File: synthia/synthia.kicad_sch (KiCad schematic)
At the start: 87 parts, among them J1 MJ-63022B, J2 SJ3-35083C-TR, J3 PJ-007, J4 SDS-50J, Q1 IRF9540N, U1 TLV272IP, U2 STM32H750ZBT6, U3 LD1117V33

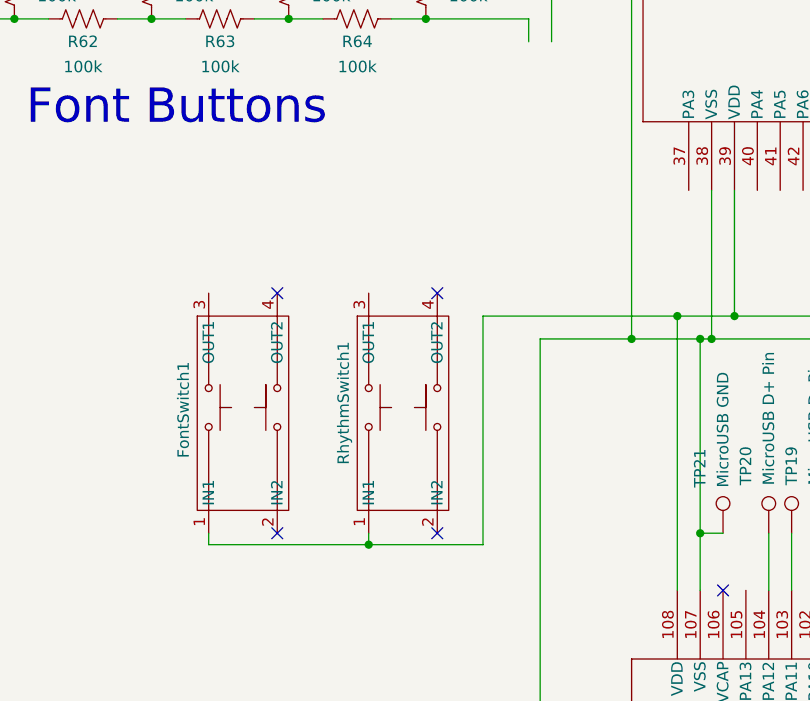
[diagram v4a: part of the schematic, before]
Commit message: added all 3D models for the footprints into the pcb design, fixed some DRC errors
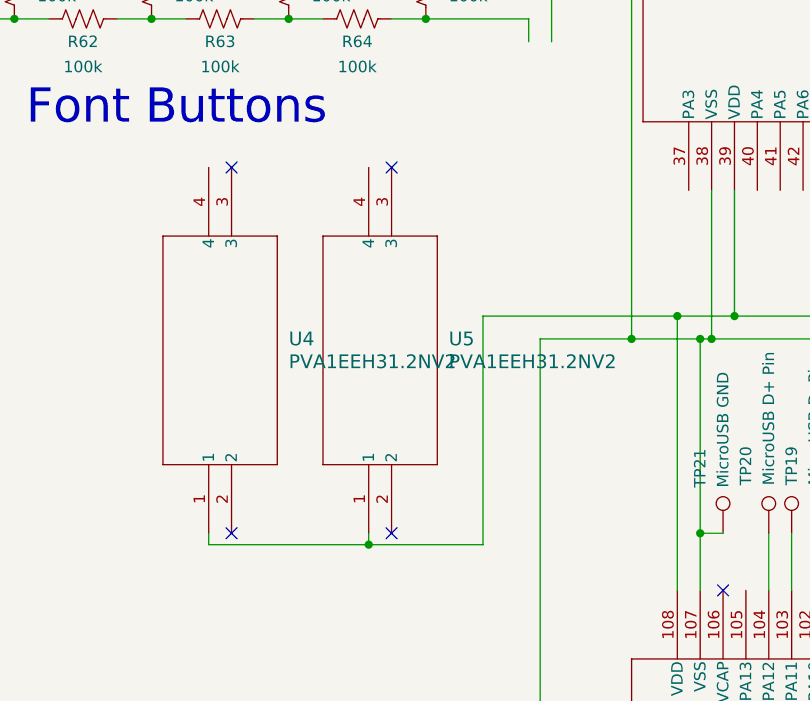
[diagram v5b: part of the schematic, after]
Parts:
- removed FontSwitch1, RhythmSwitch1: (no value), Synthia_footprint_library:Latching Switch, symbol Synthia_Symbol_Library:Latching_switch
- added U4, U5: PVA1EEH31.2NV2, SWITCH_H31.2NV2, symbol Synthia_Symbol_Library:PVA1EEH31.2NV2
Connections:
- net +3.3V: now also U4.1, U5.1
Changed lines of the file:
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@@
 	)
 	(no_connect
-		(at 60.96 199.39)
+		(at 55.88 199.39)
 	)
 	(no_connect
@@
 	)
 	(no_connect
-		(at 78.74 172.72)
+		(at 73.66 158.75)
 	)
 	(no_connect
@@
 	)
 	(no_connect
-		(at 60.96 172.72)
+		(at 55.88 158.75)
 	)
 	(no_connect
@@
 	)
 	(no_connect
-		(at 78.74 199.39)
+		(at 73.66 199.39)
 	)
 	(no_connect
@@
 	)
 	(symbol
-		(lib_id "Synthia_Symbol_Library:Latching_switch")
-		(at 62.23 181.61 0)
+		(lib_id "Synthia_Symbol_Library:PVA1EEH31.2NV2")
+		(at 53.34 199.39 90)
 		(unit 1)
 		(body_style 1)
@@
 		(in_pos_files yes)
 		(dnp no)
-		(property "Reference" "FontSwitch1"
-			(at 50.546 185.674 90)
+		(fields_autoplaced yes)
+		(property "Reference" "U4"
+			(at 62.23 177.7999 90)
 			(show_name no)
 			(do_not_autoplace no)
 			(effects
 				(font
-					(size 1.27 1.27)
+					(size 1.524 1.524)
 				)
+				(justify right)
 			)
 		)
-		(property "Value" ""
-			(at 62.23 181.61 0)
+		(property "Value" "PVA1EEH31.2NV2"
+			(at 62.23 180.3399 90)
 			(show_name no)
 			(do_not_autoplace no)
 			(effects
 				(font
-					(size 1.27 1.27)
+					(size 1.524 1.524)
 				)
+				(justify right)
 			)
 		)
-		(property "Footprint" "Synthia_footprint_library:Latching Switch"
-			(at 62.23 181.61 0)
+		(property "Footprint" "SWITCH_H31.2NV2"
+			(at 53.34 199.39 0)
 			(hide yes)
 			(show_name no)
@@
 				(font
 					(size 1.27 1.27)
+					(italic yes)
 				)
 			)
 		)
-		(property "Datasheet" ""
-			(at 62.23 181.61 0)
+		(property "Datasheet" "PVA1EEH31.2NV2"
+			(at 53.34 199.39 0)
 			(hide yes)
 			(show_name no)
@@
 				(font
 					(size 1.27 1.27)
+					(italic yes)
 				)
 			)
 		)
 		(property "Description" ""
-			(at 62.23 181.61 0)
+			(at 53.34 199.39 0)
 			(hide yes)
 			(show_name no)
@@
 			)
 		)
-		(pin "2"
-		)
 		(pin "3"
 		)
-		(pin "4"
-		)
 		(pin "1"
 		)
+		(pin "2"
+		)
+		(pin "4"
+		)
 		(instances
 			(project "synthia"
 				(path "/b7ca07b0-c23c-4333-a610-582d2798793b"
-					(reference "FontSwitch1")
+					(reference "U4")
 					(unit 1)
 				)
@@
 	)
 	(symbol
-		(lib_id "Synthia_Symbol_Library:Latching_switch")
-		(at 80.01 181.61 0)
-		(unit 1)
-		(body_style 1)
-		(exclude_from_sim no)
-		(in_bom yes)
-		(on_board yes)
-		(in_pos_files yes)
-		(dnp no)
-		(property "Reference" "RhythmSwitch1"
-			(at 68.326 191.77 90)
-			(show_name no)
-			(do_not_autoplace no)
-			(effects
-				(font
-					(size 1.27 1.27)
-				)
-				(justify left)
-			)
-		)
-		(property "Value" ""
-			(at 80.01 181.61 0)
-			(show_name no)
-			(do_not_autoplace no)
-			(effects
-				(font
-					(size 1.27 1.27)
-				)
-			)
-		)
-		(property "Footprint" "Synthia_footprint_library:Latching Switch"
-			(at 80.01 181.61 0)
-			(hide yes)
-			(show_name no)
-			(do_not_autoplace no)
-			(effects
-				(font
-					(size 1.27 1.27)
-				)
-			)
-		)
-		(property "Datasheet" ""
-			(at 80.01 181.61 0)
-			(hide yes)
-			(show_name no)
-			(do_not_autoplace no)
-			(effects
-				(font
-					(size 1.27 1.27)
-				)
-			)
-		)
-		(property "Description" ""
-			(at 80.01 181.61 0)
-			(hide yes)
-			(show_name no)
-			(do_not_autoplace no)
-			(effects
-				(font
-					(size 1.27 1.27)
-				)
-			)
-		)
-		(pin "2"
-		)
-		(pin "3"
-		)
-		(pin "4"
-		)
-		(pin "1"
-		)
-		(instances
-			(project "synthia"
-				(path "/b7ca07b0-c23c-4333-a610-582d2798793b"
-					(reference "RhythmSwitch1")
-					(unit 1)
-				)
-			)
-		)
-	)
-	(symbol
 		(lib_id "Connector:TestPoint")
 		(at 373.38 77.47 270)
@@
 					(unit 1)
 				)
+			)
+		)
+	)
+	(symbol
+		(lib_id "Synthia_Symbol_Library:PVA1EEH31.2NV2")
+		(at 71.12 199.39 90)
+		(unit 1)
+		(body_style 1)
+		(exclude_from_sim no)
+		(in_bom yes)
+		(on_board yes)
+		(in_pos_files yes)
+		(dnp no)
+		(fields_autoplaced yes)
+		(property "Reference" "U5"
+			(at 80.01 177.7999 90)
+			(show_name no)
+			(do_not_autoplace no)
+			(effects
+				(font
+					(size 1.524 1.524)
+				)
+				(justify right)
+			)
+		)
+		(property "Value" "PVA1EEH31.2NV2"
+			(at 80.01 180.3399 90)
+			(show_name no)
+			(do_not_autoplace no)
+			(effects
+				(font
+					(size 1.524 1.524)
+				)
+				(justify right)
+			)
+		)
+		(property "Footprint" "SWITCH_H31.2NV2"
+			(at 71.12 199.39 0)
+			(hide yes)
+			(show_name no)
+			(do_not_autoplace no)
+			(effects
+				(font
+					(size 1.27 1.27)
+					(italic yes)
+				)
+			)
+		)
+		(property "Datasheet" "PVA1EEH31.2NV2"
+			(at 71.12 199.39 0)
+			(hide yes)
+			(show_name no)
+			(do_not_autoplace no)
+			(effects
+				(font
+					(size 1.27 1.27)
+					(italic yes)
+				)
+			)
+		)
+		(property "Description" ""
+			(at 71.12 199.39 0)
+			(hide yes)
+			(show_name no)
+			(do_not_autoplace no)
+			(effects
+				(font
+					(size 1.27 1.27)
+				)
+			)
+		)
+		(pin "3"
+		)
+		(pin "1"
+		)
+		(pin "2"
+		)
+		(pin "4"
+		)
+		(instances
+			(project "synthia"
+				(path "/b7ca07b0-c23c-4333-a610-582d2798793b"
+					(reference "U5")
+					(unit 1)
+				)

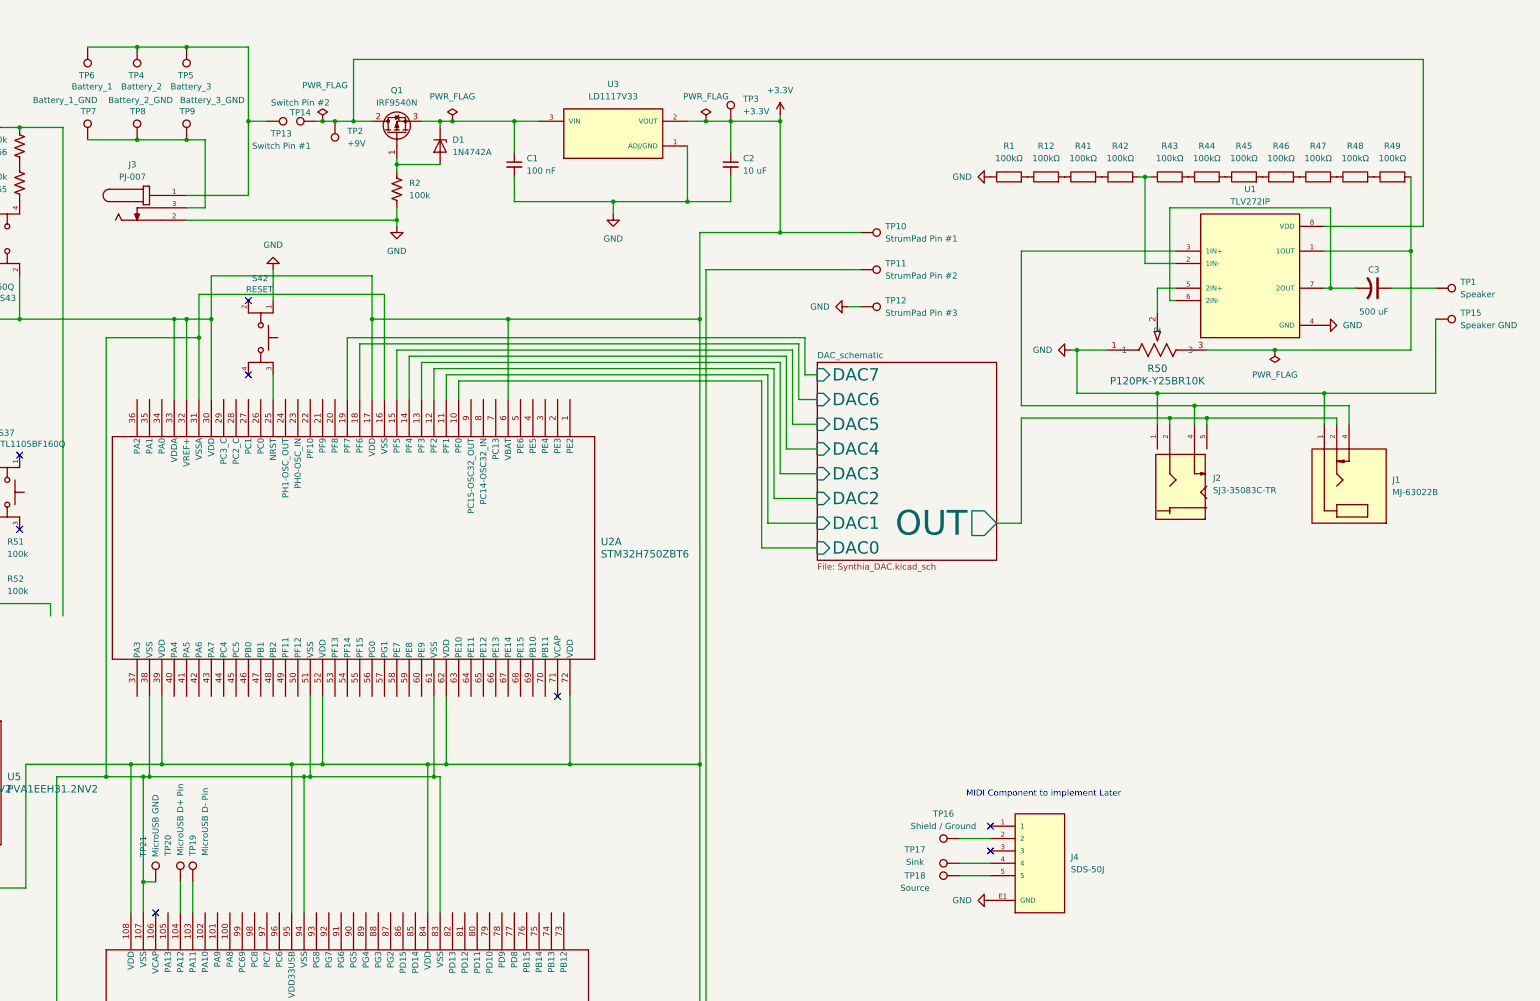
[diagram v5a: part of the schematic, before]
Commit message: continued PCB Work, Power circuit is wired
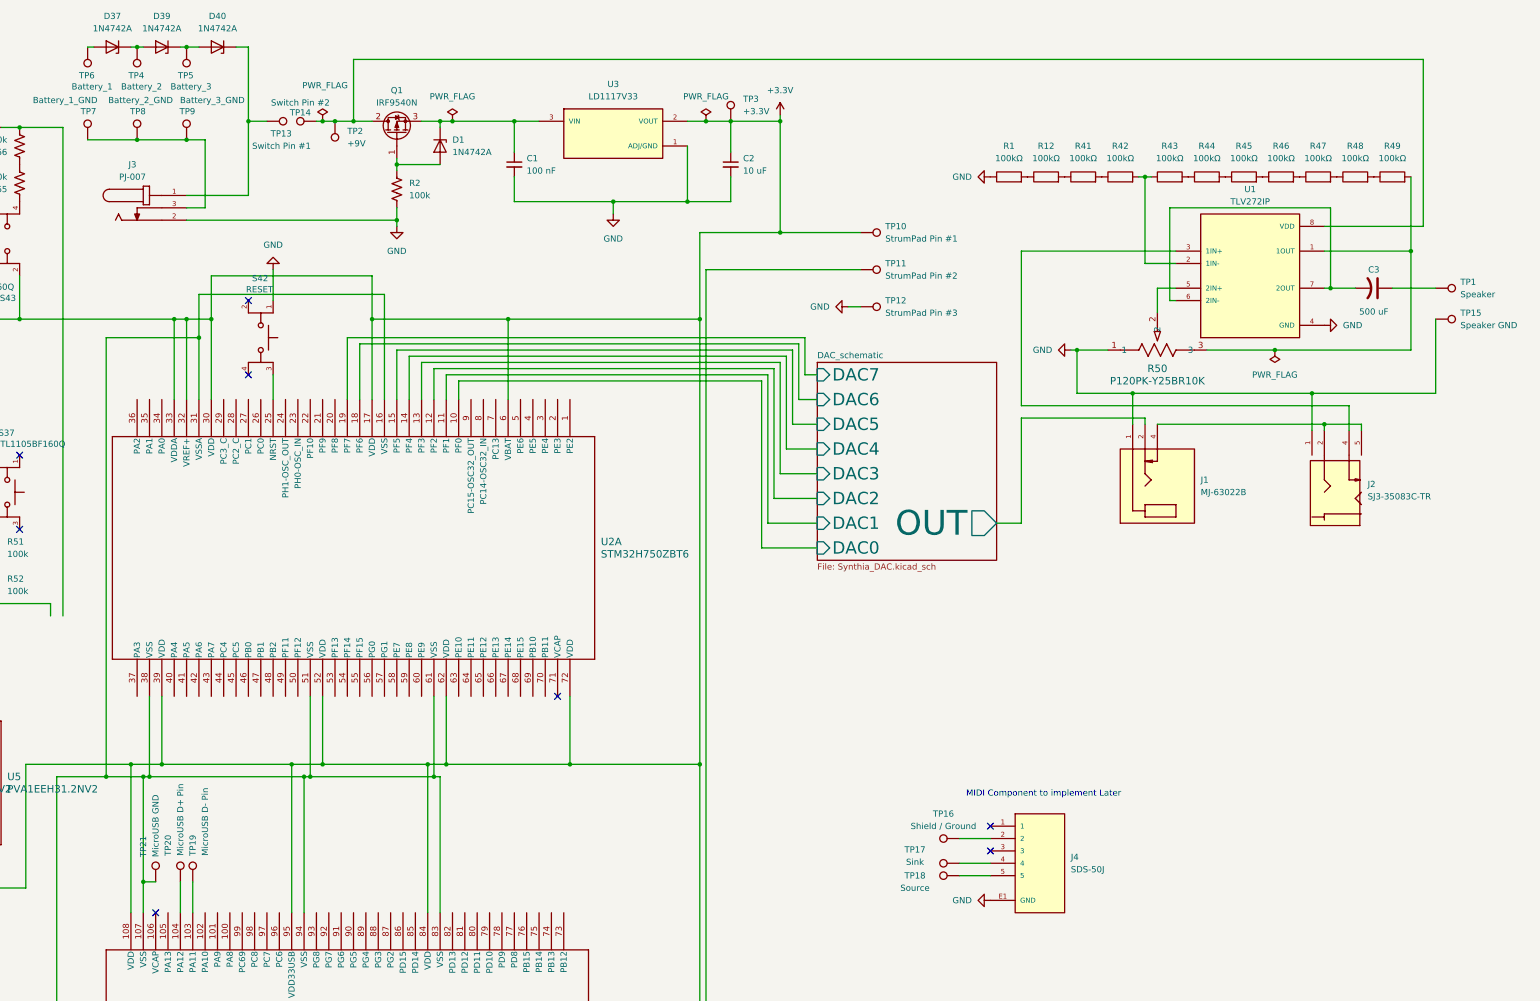
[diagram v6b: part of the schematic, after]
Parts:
- added D37, D39, D40: 1N4742A, Diode_THT:D_DO-41_SOD81_P10.16mm_Horizontal, symbol Diode:1N47xxA
- U4, U5: footprint SWITCH_H31.2NV2 -> Synthia_footprint_library:SWITCH_H31.2NV2
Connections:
- net DAC_schematic/OUT: no longer J2.2, J2.5
- net at J2.4, U1.3 (1IN+): no longer J1.4
- new net: D40.1 (K), J3.1, TP13.1
- new net: D39.1 (K), D40.2 (A), TP5.1
- new net: D37.1 (K), D39.2 (A), TP4.1
- new net: D37.2 (A), TP6.1
- new net: J1.4, J2.2, J2.5
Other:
- moved on the sheet: J1, J2

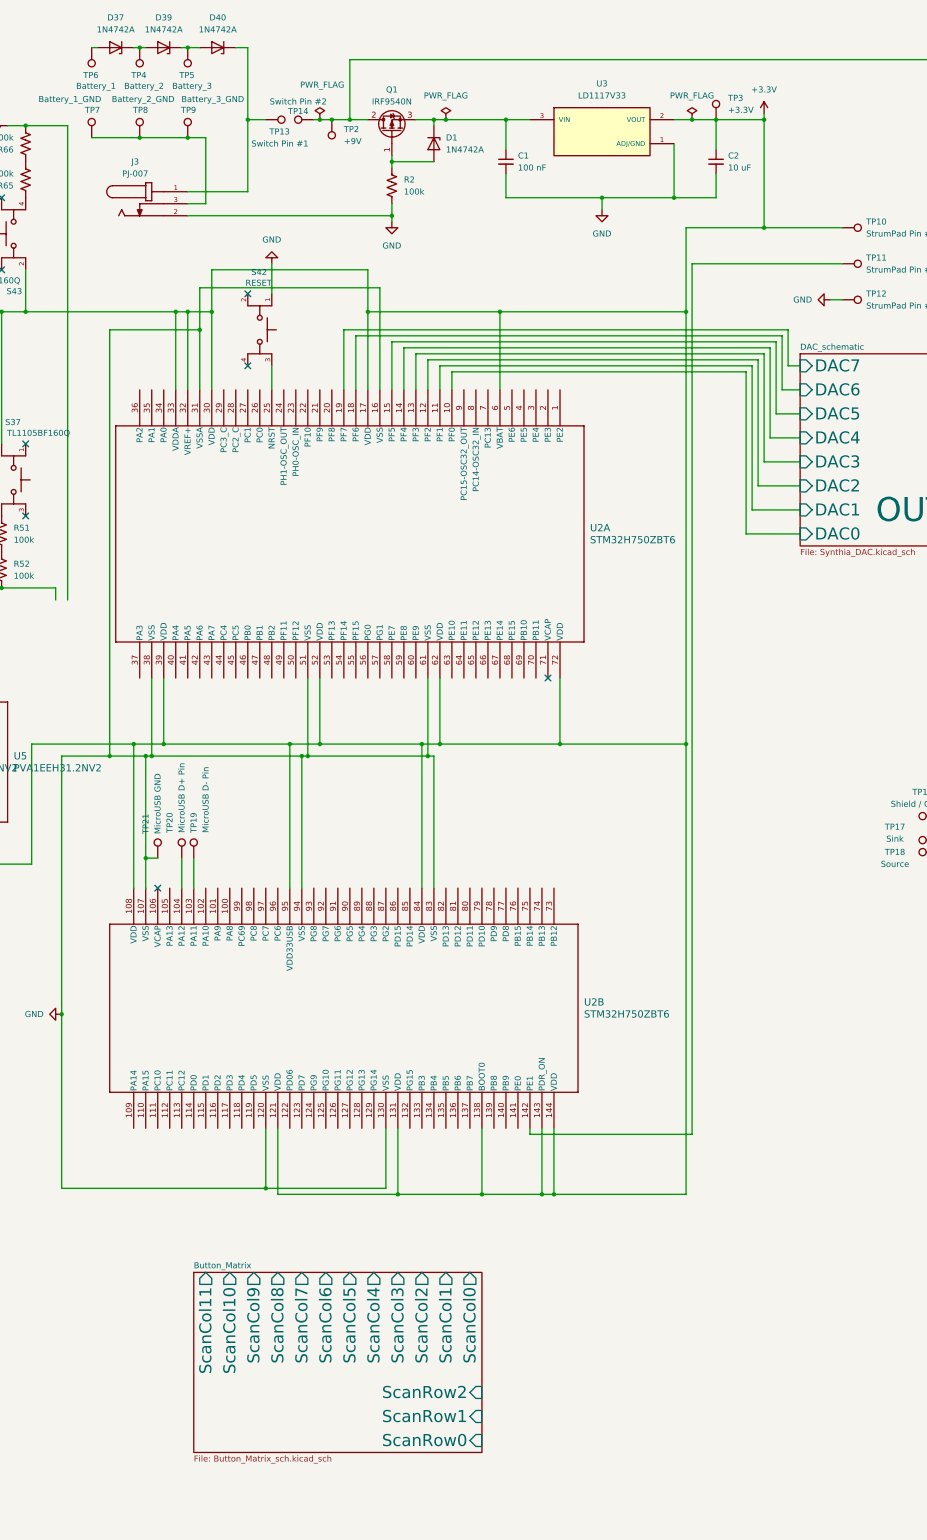
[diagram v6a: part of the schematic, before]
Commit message: More PCB Work, Button Matrix fully routed and strumpad wiring done
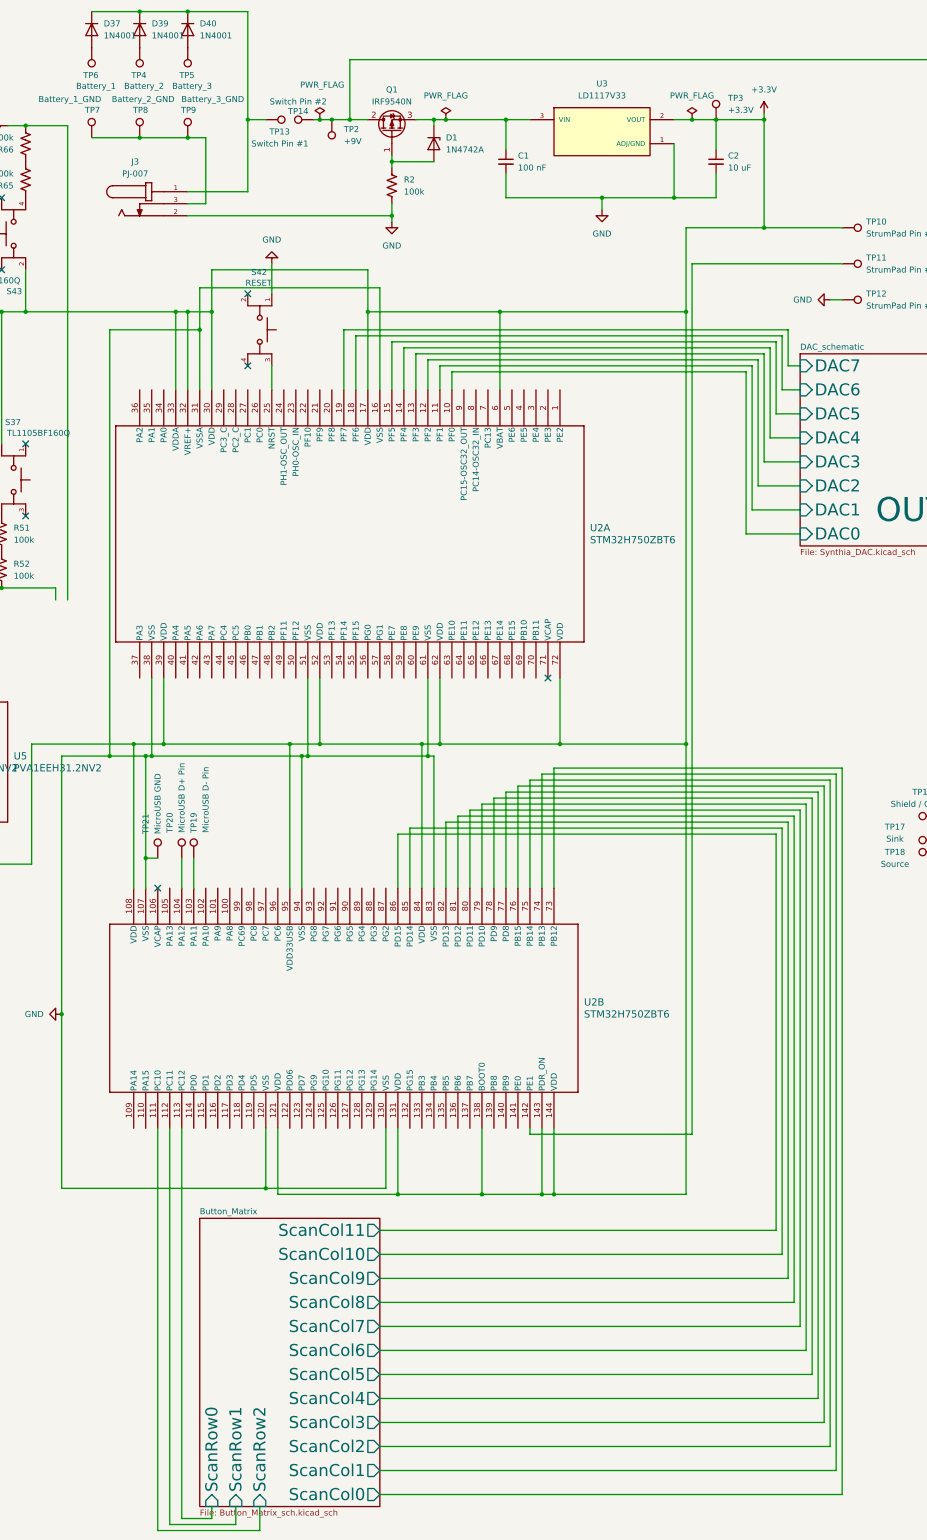
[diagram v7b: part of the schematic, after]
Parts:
- removed D37, D39, D40: 1N4742A, Diode_THT:D_DO-41_SOD81_P10.16mm_Horizontal, symbol Diode:1N47xxA
- added D37, D39, D40: 1N4001, Diode_THT:D_DO-41_SOD81_P10.16mm_Horizontal, symbol Diode:1N4001
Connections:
- net Button_Matrix/ScanCol0: now also U2.73 (PB12)
- net Button_Matrix/ScanCol1: now also U2.74 (PB13)
- net Button_Matrix/ScanCol10: now also U2.85 (PD14)
- net Button_Matrix/ScanCol11: now also U2.86 (PD15)
- net Button_Matrix/ScanCol2: now also U2.75 (PB14)
- net Button_Matrix/ScanCol3: now also U2.76 (PB15)
- net Button_Matrix/ScanCol4: now also U2.77 (PD8)
- net Button_Matrix/ScanCol5: now also U2.78 (PD9)
- net Button_Matrix/ScanCol6: now also U2.79 (PD10)
- net Button_Matrix/ScanCol7: now also U2.80 (PD11)
- net Button_Matrix/ScanCol8: now also U2.81 (PD12)
- net Button_Matrix/ScanCol9: now also U2.82 (PD13)
- net Button_Matrix/ScanRow0: now also U2.113 (PC12)
- net Button_Matrix/ScanRow1: now also U2.112 (PC11)
- net Button_Matrix/ScanRow2: now also U2.111 (PC10)
- net at J3.1, TP13.1: now also D37.1 (K), D39.1 (K), D40.1 (K)
- net at TP5.1: now also D40.2 (A)
- net at TP4.1: now also D39.2 (A)
- net at TP6.1: now also D37.2 (A)
